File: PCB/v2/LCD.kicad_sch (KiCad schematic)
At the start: 1 part

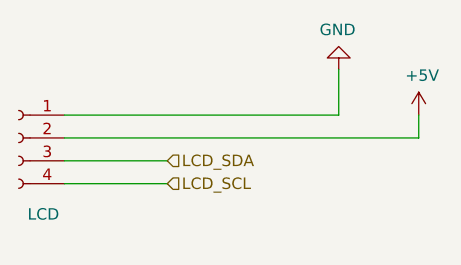
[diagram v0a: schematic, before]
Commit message: WIP updated symbols for tmc5106
Updated footprint for tmc5106,
need to check how motor wiring is done, might be wired up stupid before and that's gonna be sad
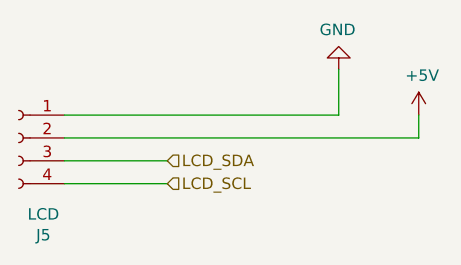
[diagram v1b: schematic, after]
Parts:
- gave numbers to parts that had none: 1
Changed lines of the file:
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@@
   (symbol (lib_id "MMTK-rescue:Conn_01x04_Female-Connector-MMTK-rescue-MMTK-rescue") (at 116.84 137.16 0) (mirror y) (unit 1)
     (in_bom yes) (on_board yes)
-    (property "Reference" "" (id 0) (at 119.5832 147.955 0))
+    (property "Reference" "J5" (id 0) (at 119.5832 147.955 0))
     (property "Value" "LCD" (id 1) (at 119.5832 145.6436 0))
     (property "Footprint" "Connector_PinSocket_2.54mm:PinSocket_1x04_P2.54mm_Horizontal" (id 2) (at 116.84 137.16 0)
@@
   (symbol (lib_id "MMTK-rescue:GND-power-MMTK-rescue-MMTK-rescue") (at 152.4 129.54 180) (unit 1)
     (in_bom yes) (on_board yes)
-    (property "Reference" "" (id 0) (at 152.4 123.19 0)
+    (property "Reference" "#PWR0147" (id 0) (at 152.4 123.19 0)
       (effects (font (size 1.27 1.27)) hide)
     )
@@
   (symbol (lib_id "MMTK-rescue:+5V-power-MMTK-rescue-MMTK-rescue") (at 161.29 134.62 0) (unit 1)
     (in_bom yes) (on_board yes)
-    (property "Reference" "" (id 0) (at 161.29 138.43 0)
+    (property "Reference" "#PWR0148" (id 0) (at 161.29 138.43 0)
       (effects (font (size 1.27 1.27)) hide)
     )
